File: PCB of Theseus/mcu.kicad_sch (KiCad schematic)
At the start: 19 parts, among them J5 Programmer, U6 STM32H750VBTx, U8 MX25L25645G

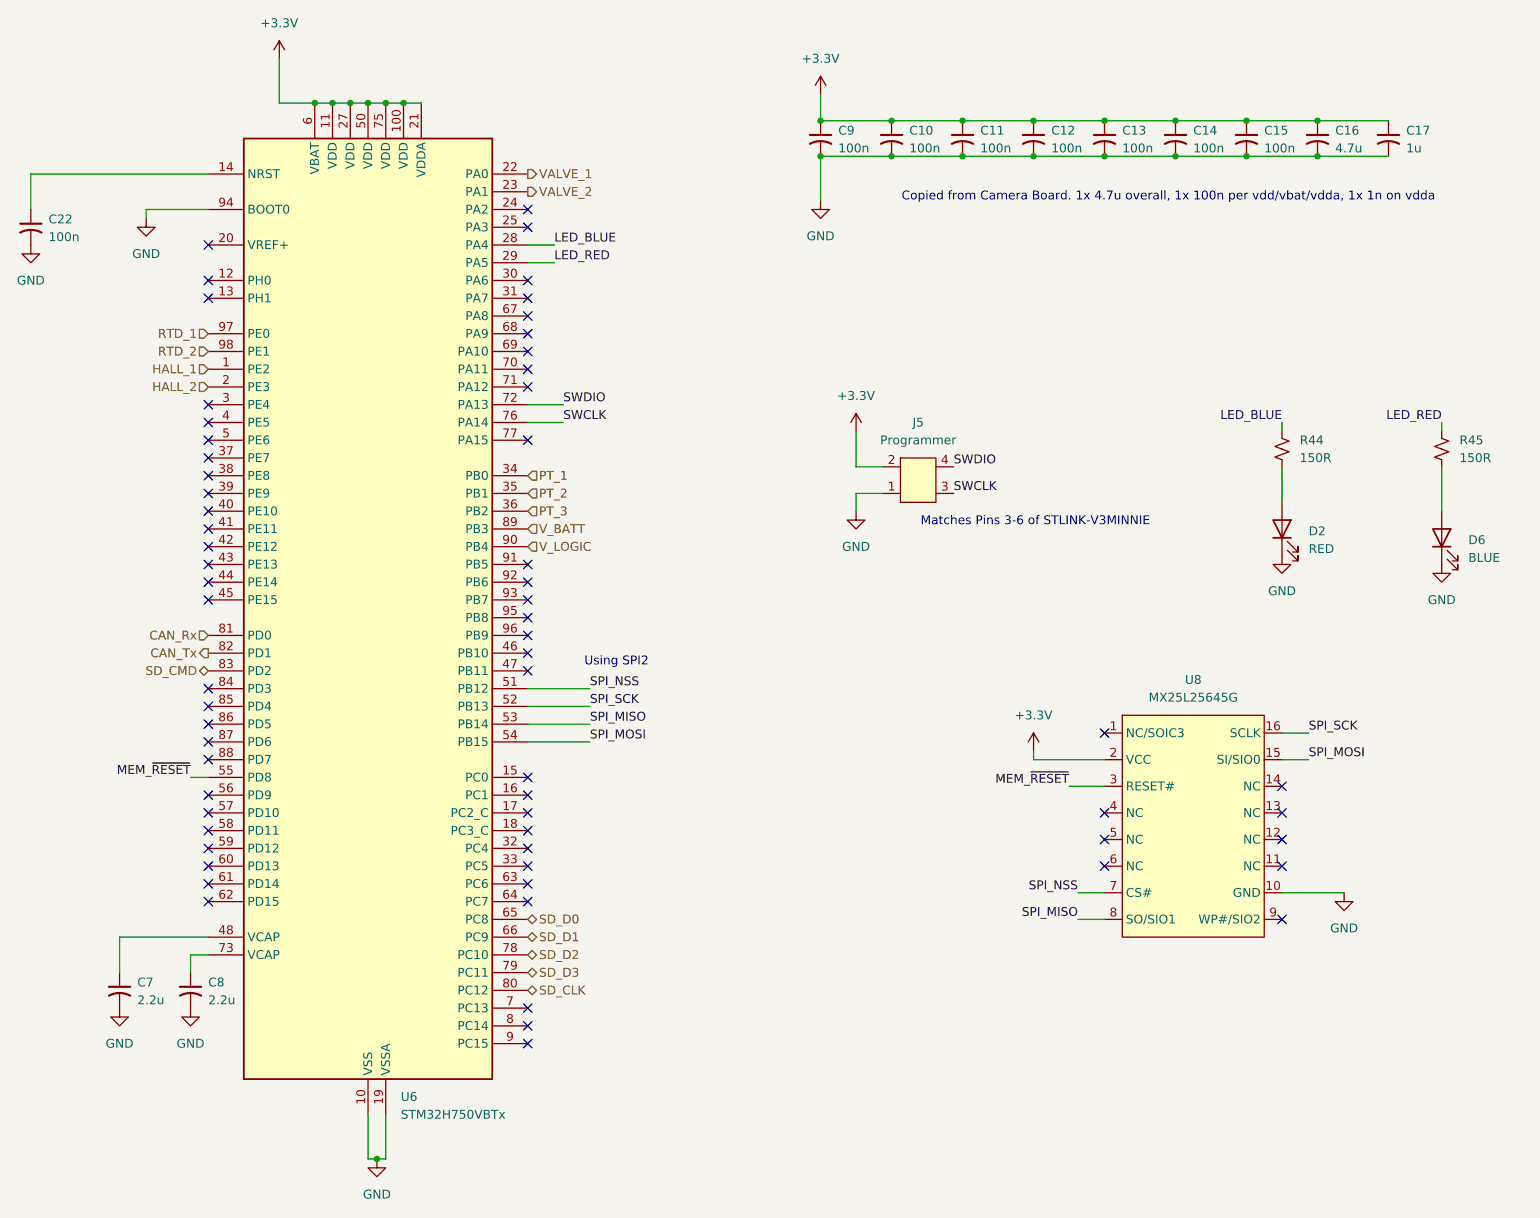
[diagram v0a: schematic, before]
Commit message: Updates to schematic, added 3rd RTD, initial PCB layout completed.
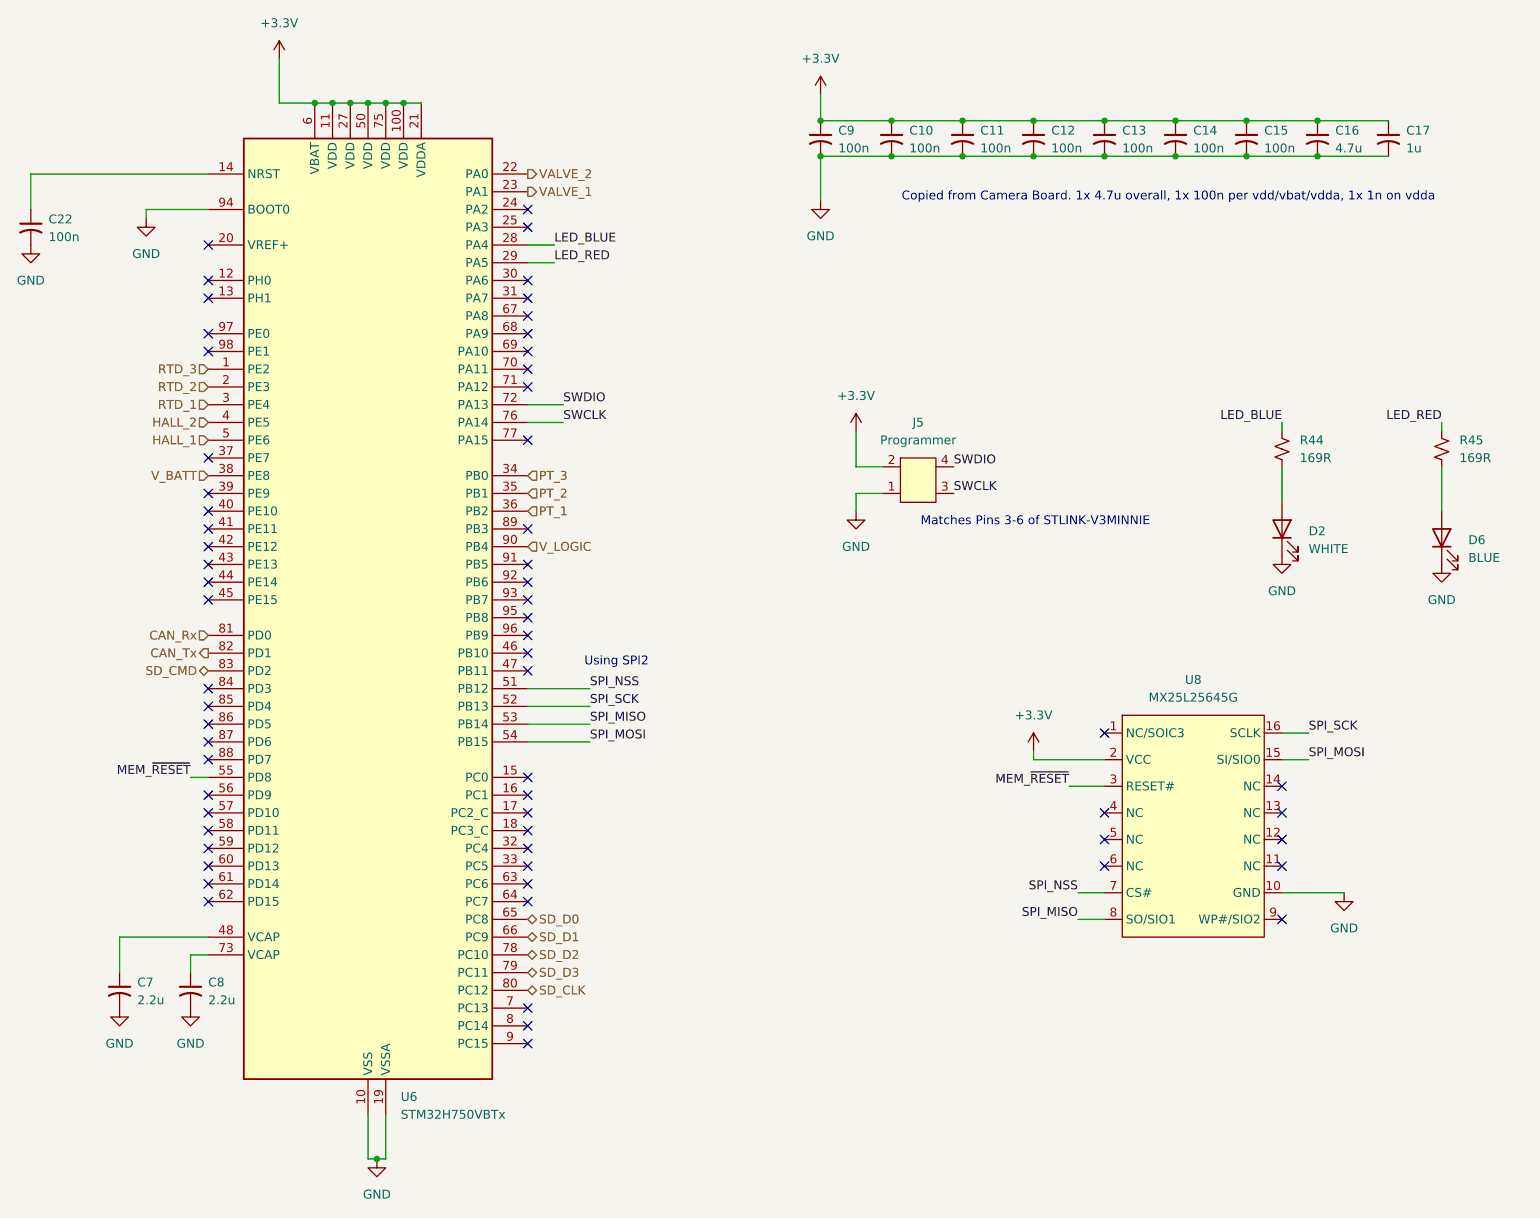
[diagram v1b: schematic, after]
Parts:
- C10, C11, C12, C13, C14, C15, C16, C22, C7, C8, C9: footprint (none) -> Capacitor_SMD:C_0603_1608Metric_Pad1.08x0.95mm_HandSolder
- C17: footprint (none) -> Capacitor_SMD:C_0402_1005Metric_Pad0.74x0.62mm_HandSolder
- D2: value RED -> WHITE; footprint (none) -> Diode_SMD:D_1206_3216Metric_Pad1.42x1.75mm_HandSolder
- D6: footprint (none) -> Diode_SMD:D_0603_1608Metric_Pad1.05x0.95mm_HandSolder
- J5: footprint (none) -> Connector_PinHeader_1.27mm:PinHeader_2x02_P1.27mm_Vertical_SMD
- R44, R45: value 150R -> 169R; footprint (none) -> Resistor_SMD:R_0603_1608Metric_Pad0.98x0.95mm_HandSolder
- U8: footprint (none) -> Package_SO:SOIC-16W_7.5x10.3mm_P1.27mm
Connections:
- net HALL_1: now also U6.5 (PE6); no longer U6.1 (PE2)
- net HALL_2: now also U6.4 (PE5); no longer U6.2 (PE3)
- net PT_1: now also U6.36 (PB2); no longer U6.34 (PB0)
- net PT_3: now also U6.34 (PB0); no longer U6.36 (PB2)
- net RTD_1: now also U6.3 (PE4); no longer U6.97 (PE0)
- net RTD_2: now also U6.2 (PE3); no longer U6.98 (PE1)
- net VALVE_1: now also U6.23 (PA1); no longer U6.22 (PA0)
- net VALVE_2: now also U6.22 (PA0); no longer U6.23 (PA1)
- net V_BATT: now also U6.38 (PE8); no longer U6.89 (PB3)
- new net RTD_3: U6.1 (PE2)
- no-connect marks 64 -> 63
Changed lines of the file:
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@@
 	)
 	(no_connect
+		(at 69.85 63.5)
+	)
+	(no_connect
 		(at 69.85 127)
 	)
@@
 	)
 	(no_connect
-		(at 69.85 71.12)
-	)
-	(no_connect
 		(at 115.57 63.5)
 	)
@@
 	)
 	(no_connect
+		(at 69.85 60.96)
+	)
+	(no_connect
 		(at 223.52 144.78)
 	)
@@
 	)
 	(no_connect
+		(at 115.57 88.9)
+	)
+	(no_connect
 		(at 69.85 139.7)
 	)
@@
 	)
 	(no_connect
-		(at 69.85 81.28)
-	)
-	(no_connect
 		(at 69.85 91.44)
 	)
@@
 	)
 	(no_connect
-		(at 69.85 73.66)
-	)
-	(no_connect
 		(at 69.85 114.3)
 	)
@@
 	)
 	(no_connect
-		(at 69.85 76.2)
-	)
-	(no_connect
 		(at 115.57 142.24)
 	)
@@
 	(hierarchical_label "V_BATT"
 		(shape input)
-		(at 115.57 88.9 0)
+		(at 69.85 81.28 180)
 		(effects
 			(font
 				(size 1.27 1.27)
 			)
-			(justify left)
+			(justify right)
 		)
 	)
 	(hierarchical_label "RTD_1"
 		(shape input)
-		(at 69.85 60.96 180)
+		(at 69.85 71.12 180)
 		(effects
 			(font
@@
 	(hierarchical_label "VALVE_2"
 		(shape output)
-		(at 115.57 40.64 0)
+		(at 115.57 38.1 0)
 		(effects
 			(font
@@
 	(hierarchical_label "HALL_1"
 		(shape input)
-		(at 69.85 66.04 180)
+		(at 69.85 76.2 180)
 		(effects
 			(font
@@
 	(hierarchical_label "HALL_2"
 		(shape input)
-		(at 69.85 68.58 180)
+		(at 69.85 73.66 180)
+		(effects
+			(font
+				(size 1.27 1.27)
+			)
+			(justify right)
+		)
+	)
+	(hierarchical_label "RTD_3"
+		(shape input)
+		(at 69.85 66.04 180)
 		(effects
 			(font
@@
 	(hierarchical_label "PT_1"
 		(shape input)
-		(at 115.57 81.28 0)
+		(at 115.57 86.36 0)
 		(effects
 			(font
@@
 	(hierarchical_label "VALVE_1"
 		(shape output)
-		(at 115.57 38.1 0)
+		(at 115.57 40.64 0)
 		(effects
 			(font
@@
 	(hierarchical_label "RTD_2"
 		(shape input)
-		(at 69.85 63.5 180)
+		(at 69.85 68.58 180)
 		(effects
 			(font
@@
 	(hierarchical_label "PT_3"
 		(shape input)
-		(at 115.57 86.36 0)
+		(at 115.57 81.28 0)
 		(effects
 			(font
@@
 			)
 		)
-		(property "Value" "150R"
+		(property "Value" "169R"
 			(at 248.92 78.7399 0)
 			(effects
@@
 			)
 		)
-		(property "Footprint" ""
+		(property "Footprint" "Resistor_SMD:R_0603_1608Metric_Pad0.98x0.95mm_HandSolder"
 			(at 246.38 77.47 0)
 			(effects
@@
 			)
 		)
-		(property "Value" "RED"
+		(property "Value" "WHITE"
 			(at 227.33 91.7574 90)
 			(effects
@@
 			)
 		)
-		(property "Footprint" ""
+		(property "Footprint" "Diode_SMD:D_1206_3216Metric_Pad1.42x1.75mm_HandSolder"
 			(at 223.52 88.9 0)
 			(effects
@@
 			)
 		)
-		(property "Footprint" ""
+		(property "Footprint" "Capacitor_SMD:C_0603_1608Metric_Pad1.08x0.95mm_HandSolder"
 			(at 167.64 33.02 0)
 			(effects
@@
 			)
 		)
-		(property "Footprint" ""
+		(property "Footprint" "Capacitor_SMD:C_0603_1608Metric_Pad1.08x0.95mm_HandSolder"
 			(at 57.15 154.94 0)
 			(effects
@@
 			)
 		)
-		(property "Footprint" ""
+		(property "Footprint" "Capacitor_SMD:C_0603_1608Metric_Pad1.08x0.95mm_HandSolder"
 			(at 208.28 33.02 0)
 			(effects
@@
 			)
 		)
-		(property "Footprint" ""
+		(property "Footprint" "Capacitor_SMD:C_0603_1608Metric_Pad1.08x0.95mm_HandSolder"
 			(at 157.48 33.02 0)
 			(effects
@@
 			)
 		)
-		(property "Footprint" ""
+		(property "Footprint" "Connector_PinHeader_1.27mm:PinHeader_2x02_P1.27mm_Vertical_SMD"
 			(at 171.45 78.74 0)
 			(effects
@@
 			)
 		)
-		(property "Value" "150R"
+		(property "Value" "169R"
 			(at 226.06 78.7399 0)
 			(effects
@@
 			)
 		)
-		(property "Footprint" ""
+		(property "Footprint" "Resistor_SMD:R_0603_1608Metric_Pad0.98x0.95mm_HandSolder"
 			(at 223.52 77.47 0)
 			(effects
@@
 			)
 		)
-		(property "Footprint" ""
+		(property "Footprint" "Capacitor_SMD:C_0603_1608Metric_Pad1.08x0.95mm_HandSolder"
 			(at 67.31 154.94 0)
 			(effects
@@
 			)
 		)
-		(property "Footprint" ""
+		(property "Footprint" "Capacitor_SMD:C_0603_1608Metric_Pad1.08x0.95mm_HandSolder"
 			(at 44.45 45.72 0)
 			(effects
@@
 			)
 		)
-		(property "Footprint" ""
+		(property "Footprint" "Capacitor_SMD:C_0402_1005Metric_Pad0.74x0.62mm_HandSolder"
 			(at 238.76 33.02 0)
 			(effects
@@
 			)
 		)
-		(property "Footprint" ""
+		(property "Footprint" "Capacitor_SMD:C_0603_1608Metric_Pad1.08x0.95mm_HandSolder"
 			(at 177.8 33.02 0)
 			(effects
@@
 			)
 		)
-		(property "Footprint" ""
+		(property "Footprint" "Capacitor_SMD:C_0603_1608Metric_Pad1.08x0.95mm_HandSolder"
 			(at 218.44 33.02 0)
 			(effects
@@
 			)
 		)
-		(property "Footprint" ""
+		(property "Footprint" "Capacitor_SMD:C_0603_1608Metric_Pad1.08x0.95mm_HandSolder"
 			(at 198.12 33.02 0)
 			(effects
@@
 			)
 		)
-		(property "Footprint" ""
+		(property "Footprint" "Capacitor_SMD:C_0603_1608Metric_Pad1.08x0.95mm_HandSolder"
 			(at 187.96 33.02 0)
 			(effects
@@
 			)
 		)
-		(property "Footprint" ""
+		(property "Footprint" "Capacitor_SMD:C_0603_1608Metric_Pad1.08x0.95mm_HandSolder"
 			(at 228.6 33.02 0)
 			(effects
@@
 			)
 		)
-		(property "Footprint" ""
+		(property "Footprint" "Package_SO:SOIC-16W_7.5x10.3mm_P1.27mm"
 			(at 210.82 111.76 0)
 			(effects
@@
 			)
 		)
-		(property "Footprint" ""
+		(property "Footprint" "Diode_SMD:D_0603_1608Metric_Pad1.05x0.95mm_HandSolder"
 			(at 246.38 90.17 0)
 			(effects
